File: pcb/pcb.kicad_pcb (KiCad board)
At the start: 2 copper layers, 161.8 x 93 mm, 59 parts, among them J1 N!N, J2 Conn_01x02_Socket, J4 Display_nice-view, J8 Conn_01x12_Socket, J9 Conn_01x12_Socket, SW1 Switch, SW10 Switch, SW11 Switch, SW12 Switch, SW13 Switch, SW14 Switch, SW15 Switch, SW16 Switch, SW17 Switch, SW18 Switch, SW19 Switch, SW2 Switch, SW20 Switch, SW21 SW_Push, SW22 SW_SPDT, SW3 Switch, SW4 Switch, SW5 Switch, SW6 Switch, SW7 Switch, SW8 Switch, SW9 Switch

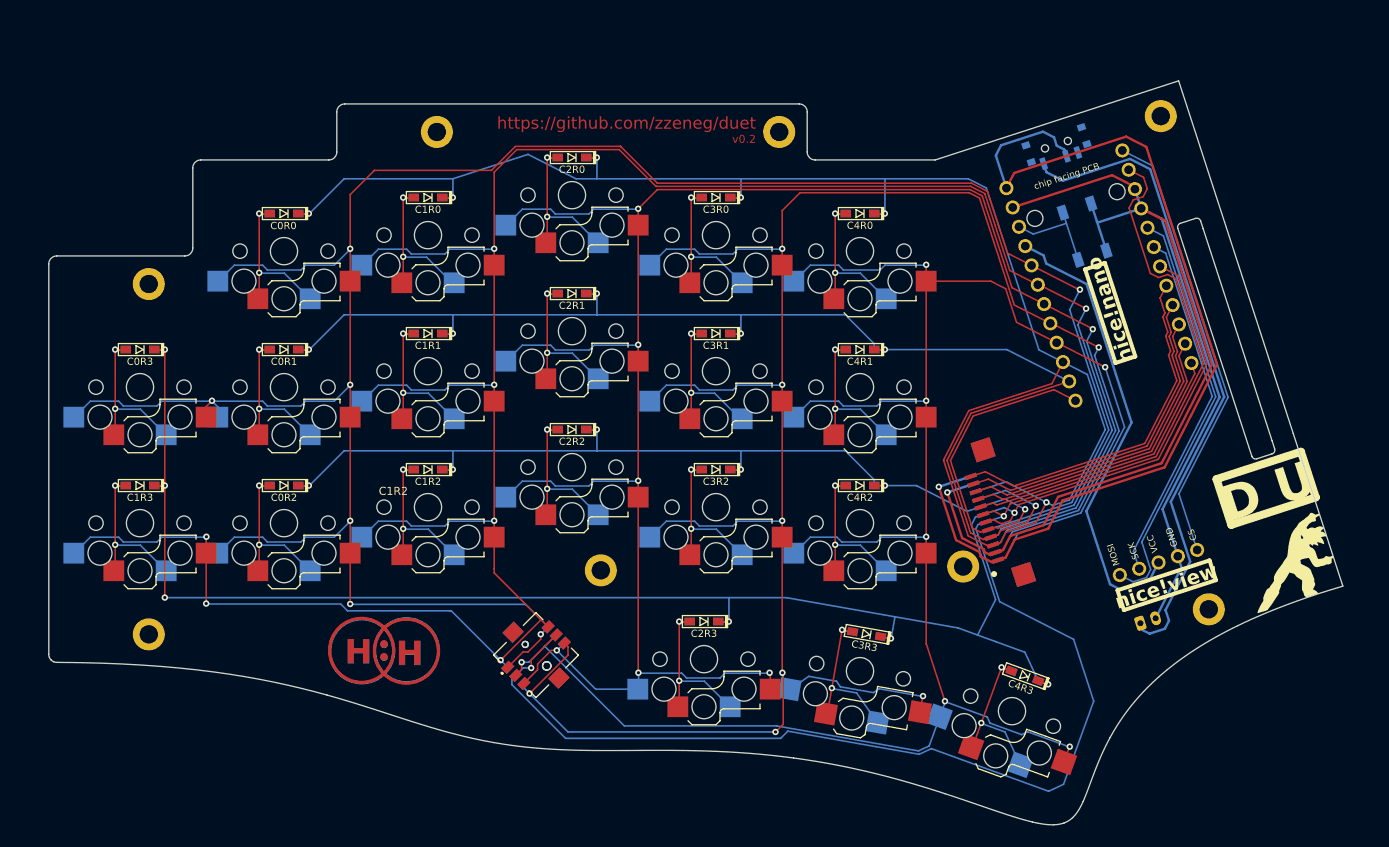
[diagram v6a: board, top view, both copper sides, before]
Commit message: revert shape changes to pcb
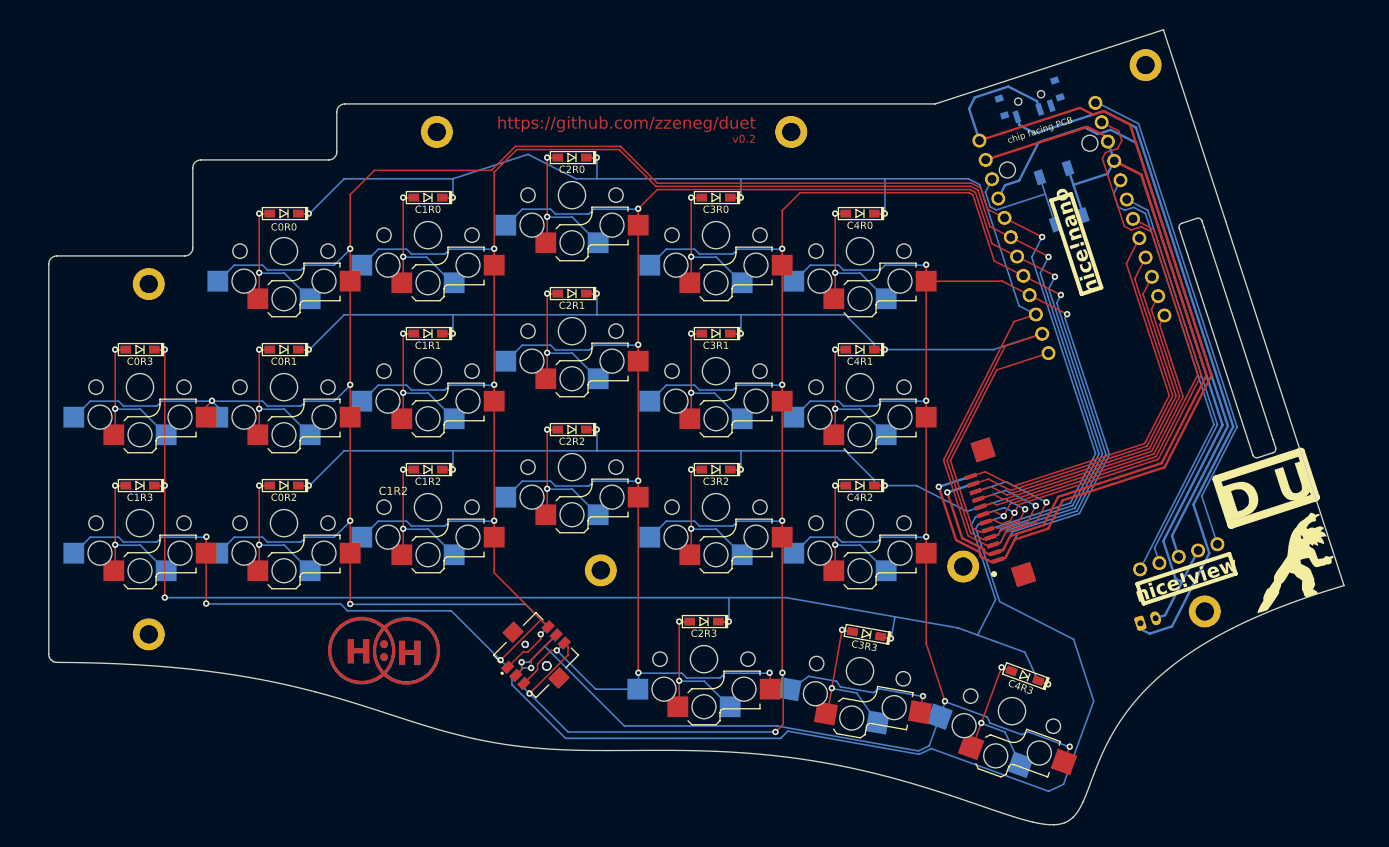
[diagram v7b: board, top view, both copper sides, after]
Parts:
- D1: moved to B.Cu
- moved J1 6.84 mm to (163.6, 54.9)
- moved SW22 6.74 mm to (158.8, 40.2)
- moved H4 6.66 mm to (173.2, 35.7)
- moved SW21 5.28 mm to (162.7, 52.1)
- moved J4 2.63 mm to (172.3, 81.5)
- moved H3 1.50 mm to (128.9, 44.1)
- moved H8 0.57 mm to (180.6, 104.0)
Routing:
- net row0: track 213.7 -> 184.2 mm
- net +3.3V: track 57.3 -> 77.6 mm
- net GND: track 164.0 -> 183.3 mm
- net BATIN: track 80.8 -> 88.6 mm
- net row4: track 193.0 -> 199.7 mm
- net row3: track 234.4 -> 240.8 mm
- net CS: track 55.6 -> 61.9 mm
- net col0_r: track 34.8 -> 40.9 mm
- net col2_r: track 39.4 -> 45.5 mm
- net col1_r: track 37.1 -> 43.2 mm
- net col3_r: track 41.6 -> 47.8 mm
- net col4_r: track 43.9 -> 50.1 mm
- net SCK: track 44.5 -> 50.4 mm
- net RST: track 12.6 -> 17.2 mm
- net MOSI: track 52.1 -> 55.4 mm
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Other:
- board size 161.8 x 93 mm -> 161.9 x 99.4 mm

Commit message: change angle to 20
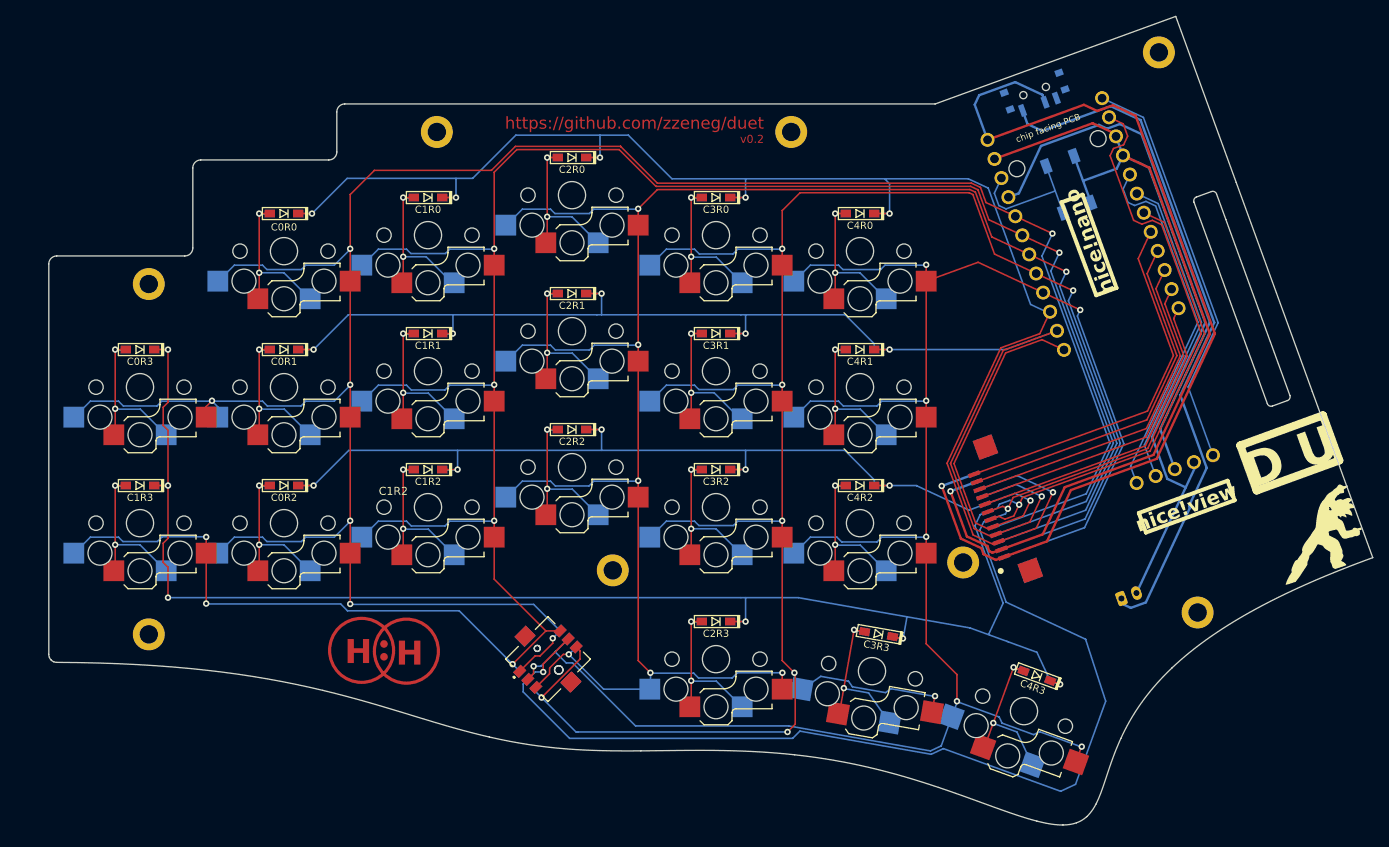
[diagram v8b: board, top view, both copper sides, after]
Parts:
- moved J4 10.8 mm to (171.2, 70.8), turned to 20 degrees
- moved G*** 5.00 mm to (193.9, 94.4)
- moved G*** 4.95 mm to (193.9, 94.4)
- moved J2 3.89 mm to (170.2, 102.4), turned to 20 degrees
- moved H4 2.30 mm to (174.9, 34.2)
- moved SW21 1.72 mm to (163.6, 50.7), turned to -70 degrees
- moved S1 1.58 mm to (98.5, 110.0)
- moved S2 1.58 mm to (98.5, 110.0)
- moved D18 1.50 mm to (119.5, 105.3)
- moved D19 1.50 mm to (139.8, 106.9)
- moved SW18 1.50 mm to (119.5, 110.0)
- moved SW19 1.50 mm to (139.0, 111.5)
- moved SW20 1.50 mm to (158.0, 116.5)
- moved D20 1.50 mm to (159.6, 112.1)
- moved H6 1.50 mm to (106.6, 98.9)
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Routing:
- net row0: track 184.2 -> 195.6 mm
- net +3.3V: track 77.6 -> 66.5 mm
- net CS: track 61.9 -> 50.9 mm
- net SCK: track 50.4 -> 39.8 mm
- net MOSI: track 55.4 -> 45.1 mm
- net row1: track 163.1 -> 171.6 mm
- net row2: track 150.6 -> 159.1 mm
- net col4: track 251.1 -> 256.1 mm
- net GND: track 183.3 -> 178.6 mm
- net col1: track 308.3 -> 313.0 mm
- net row3: track 240.8 -> 245.5 mm
- net col0: track 303.5 -> 307.4 mm
- net col2: track 253.3 -> 256.1 mm
- net col4_r: track 50.1 -> 47.3 mm
- net col3: track 267.7 -> 270.4 mm
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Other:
- board size 161.9 x 99.4 mm -> 165.5 x 101.1 mm
